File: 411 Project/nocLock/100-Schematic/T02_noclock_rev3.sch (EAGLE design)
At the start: 57 parts, among them J1 ICSP, J3 5BC-3-CA-F, J4 640455-2, J5 640455-2, J6 640455-2, J7 640455-2, J8 640455-2, Q1 DMN63D8LDW-7, Q3 DMG1012UW-7, U1 ATMEGA88A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

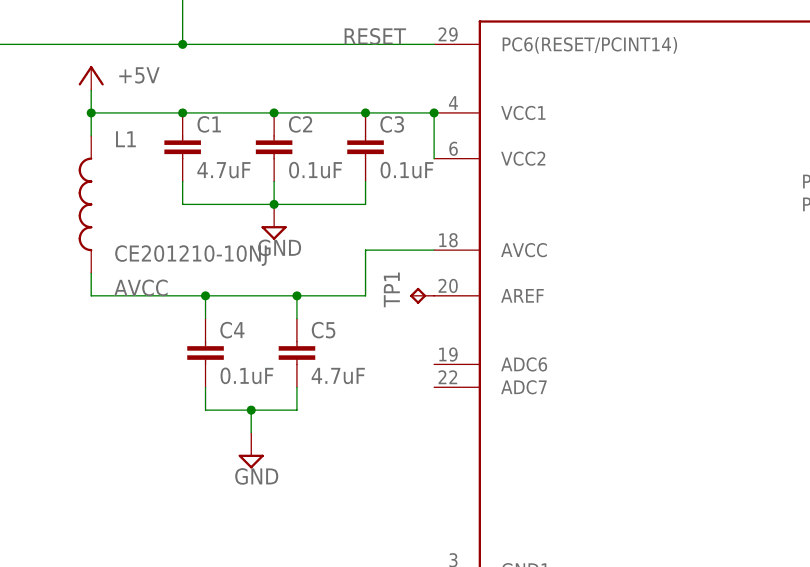
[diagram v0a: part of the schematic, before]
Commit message: Board revision
Fixed various issues with current layout, aded logo, and team name.
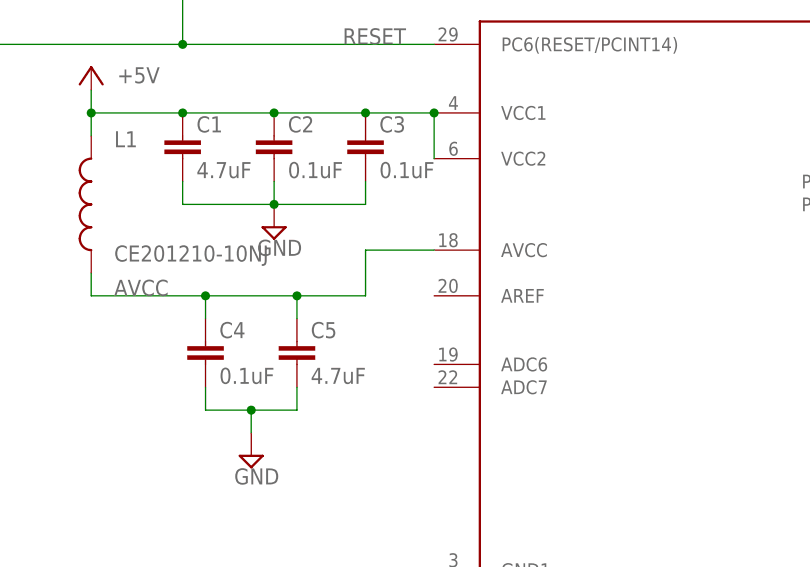
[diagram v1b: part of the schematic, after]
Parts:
- removed TP1: TPTP19R, testpad:TPTP19R
- U1: device nocLock_temp:ATMEGA88A -> T02_nocLock:ATMEGA88A; PARTNUM ATMEGA88A-AUR -> (none)
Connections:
- removed net N$13: TP1.TP, U1.AREF
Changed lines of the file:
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@@
 <parts>
 <part name="FRAME1" library="frames" deviceset="FRAME_B_L" device=""/>
-<part name="U1" library="nocLock_temp" deviceset="ATMEGA88A" device="">
-<attribute name="PARTNUM" value="ATMEGA88A-AUR "/>
-</part>
 <part name="P+2" library="supply1" deviceset="+5V" device=""/>
 <part name="C1" library="rcl" deviceset="C-EU" device="C0805" value="4.7uF">
@@
 <attribute name="PARTNUM" value="PMEG2005CT,215"/>
 </part>
-<part name="TP1" library="testpad" deviceset="TP" device="TP19R"/>
 <part name="SUPPLY18" library="supply2" deviceset="GND" device=""/>
 <part name="SUPPLY19" library="supply2" deviceset="GND" device=""/>
@@
 <part name="U$1" library="supply1" deviceset="+9V" device=""/>
 <part name="U$4" library="T02_nocLock" deviceset="+9V" device=""/>
+<part name="U1" library="T02_nocLock" deviceset="ATMEGA88A" device=""/>
 </parts>
 <sheets>
@@
 <instance part="FRAME1" gate="G$1" x="66.04" y="30.48"/>
 <instance part="FRAME1" gate="G$2" x="391.16" y="30.48"/>
-<instance part="U1" gate="G$1" x="266.7" y="180.34">
-<attribute name="PARTNUM" x="266.7" y="180.34" size="1.778" layer="96" display="off"/>
-</instance>
 <instance part="P+2" gate="1" x="193.04" y="208.28" smashed="yes">
 <attribute name="VALUE" x="200.66" y="208.28" size="1.778" layer="96" rot="R180"/>
@@
 <attribute name="PARTNUM" x="121.92" y="101.6" size="1.778" layer="96" display="off"/>
 </instance>
-<instance part="TP1" gate="G$1" x="228.6" y="182.88" rot="R90"/>
 <instance part="U2" gate="E" x="449.58" y="116.84"/>
 <instance part="U2" gate="F" x="449.58" y="88.9"/>
@@
 <instance part="U$1" gate="G$1" x="279.4" y="114.3"/>
 <instance part="U$4" gate="G$1" x="152.4" y="121.92"/>
+<instance part="U1" gate="G$1" x="266.7" y="180.34"/>
 </instances>
 <busses>
@@
 </segment>
 <segment>
-<pinref part="U1" gate="G$1" pin="GND1"/>
 <wire x1="231.14" y1="152.4" x2="228.6" y2="152.4" width="0.1524" layer="91"/>
 <wire x1="228.6" y1="152.4" x2="228.6" y2="149.86" width="0.1524" layer="91"/>
-<pinref part="U1" gate="G$1" pin="GND2"/>
 <wire x1="228.6" y1="149.86" x2="228.6" y2="147.32" width="0.1524" layer="91"/>
 <wire x1="228.6" y1="147.32" x2="228.6" y2="134.62" width="0.1524" layer="91"/>
 <wire x1="231.14" y1="149.86" x2="228.6" y2="149.86" width="0.1524" layer="91"/>
 <junction x="228.6" y="149.86"/>
-<pinref part="U1" gate="G$1" pin="GND3"/>
 <wire x1="228.6" y1="147.32" x2="231.14" y2="147.32" width="0.1524" layer="91"/>
 <junction x="228.6" y="147.32"/>
 <pinref part="SUPPLY14" gate="GND" pin="GND"/>
+<pinref part="U1" gate="G$1" pin="GND1"/>
+<pinref part="U1" gate="G$1" pin="GND2"/>
+<pinref part="U1" gate="G$1" pin="GND3"/>
 </segment>
 <segment>
@@
 <pinref part="P+2" gate="1" pin="+5V"/>
 <wire x1="193.04" y1="205.74" x2="193.04" y2="203.2" width="0.1524" layer="91"/>
-<pinref part="U1" gate="G$1" pin="VCC1"/>
 <wire x1="193.04" y1="203.2" x2="203.2" y2="203.2" width="0.1524" layer="91"/>
-<pinref part="U1" gate="G$1" pin="VCC2"/>
 <wire x1="203.2" y1="203.2" x2="213.36" y2="203.2" width="0.1524" layer="91"/>
 <wire x1="213.36" y1="203.2" x2="223.52" y2="203.2" width="0.1524" layer="91"/>
 <wire x1="223.52" y1="203.2" x2="231.14" y2="203.2" width="0.1524" layer="91"/>
 <wire x1="231.14" y1="198.12" x2="231.14" y2="203.2" width="0.1524" layer="91"/>
-<junction x="231.14" y="203.2"/>
 <pinref part="C1" gate="G$1" pin="1"/>
 <junction x="203.2" y="203.2"/>
@@
 <junction x="193.04" y="203.2"/>
 <pinref part="L1" gate="G$1" pin="2"/>
+<pinref part="U1" gate="G$1" pin="VCC1"/>
+<junction x="231.14" y="203.2"/>
+<pinref part="U1" gate="G$1" pin="VCC2"/>
 </segment>
 <segment>
@@
 <net name="AVCC" class="0">
 <segment>
-<pinref part="U1" gate="G$1" pin="AVCC"/>
 <wire x1="231.14" y1="187.96" x2="223.52" y2="187.96" width="0.1524" layer="91"/>
 <wire x1="193.04" y1="185.42" x2="193.04" y2="182.88" width="0.1524" layer="91"/>
@@
 <label x="195.58" y="182.88" size="1.778" layer="95"/>
 <pinref part="L1" gate="G$1" pin="1"/>
+<pinref part="U1" gate="G$1" pin="AVCC"/>
 </segment>
 </net>
@@
 <segment>
 <wire x1="180.34" y1="274.32" x2="180.34" y2="226.06" width="0.1524" layer="91"/>
-<pinref part="U1" gate="G$1" pin="PB0(PCINT0/CLKO/ICP1)"/>
 <pinref part="U2" gate="A" pin="O"/>
 <wire x1="180.34" y1="226.06" x2="307.34" y2="226.06" width="0.1524" layer="91"/>
@@
 <wire x1="307.34" y1="226.06" x2="307.34" y2="210.82" width="0.1524" layer="91"/>
 <wire x1="307.34" y1="210.82" x2="304.8" y2="210.82" width="0.1524" layer="91"/>
+<pinref part="U1" gate="G$1" pin="PB0(PCINT0/CLKO/ICP1)"/>
 </segment>
 </net>
@@
 <pinref part="R11" gate="G$1" pin="2"/>
 <label x="370.84" y="205.74" size="1.778" layer="95"/>
+<wire x1="304.8" y1="205.74" x2="396.24" y2="205.74" width="0.1524" layer="91"/>
 <pinref part="U1" gate="G$1" pin="PB2(PCINT2/SS/OC1B)"/>
-<wire x1="304.8" y1="205.74" x2="396.24" y2="205.74" width="0.1524" layer="91"/>
 </segment>
 </net>
@@
 <wire x1="231.14" y1="236.22" x2="231.14" y2="284.48" width="0.1524" layer="91"/>
 <wire x1="231.14" y1="284.48" x2="226.06" y2="284.48" width="0.1524" layer="91"/>
-<pinref part="U1" gate="G$1" pin="PB4(PCINT4/MISO)"/>
 <wire x1="304.8" y1="200.66" x2="325.12" y2="200.66" width="0.1524" layer="91"/>
 <wire x1="325.12" y1="200.66" x2="350.52" y2="200.66" width="0.1524" layer="91"/>
@@
 <wire x1="350.52" y1="200.66" x2="350.52" y2="99.06" width="0.1524" layer="91"/>
 <pinref part="J1" gate="G$1" pin="1"/>
+<pinref part="U1" gate="G$1" pin="PB4(PCINT4/MISO)"/>
 </segment>
 </net>
@@
 <net name="RESET" class="0">
 <segment>
-<pinref part="U1" gate="G$1" pin="PC6(RESET/PCINT14)"/>
 <wire x1="172.72" y1="210.82" x2="203.2" y2="210.82" width="0.1524" layer="91"/>
 <wire x1="203.2" y1="210.82" x2="231.14" y2="210.82" width="0.1524" layer="91"/>
@@
 <wire x1="172.72" y1="162.56" x2="162.56" y2="162.56" width="0.1524" layer="91"/>
 <pinref part="J1" gate="G$1" pin="5"/>
+<pinref part="U1" gate="G$1" pin="PC6(RESET/PCINT14)"/>
 </segment>
 </net>
 <net name="KNOCK_SENSE" class="0">
 <segment>
-<pinref part="U1" gate="G$1" pin="PC5(ADC5/SCL/PCINT13)"/>
 <wire x1="304.8" y1="172.72" x2="332.74" y2="172.72" width="0.1524" layer="91"/>
 <label x="307.34" y="172.72" size="1.778" layer="95"/>
@@
 <pinref part="J8" gate="G$1" pin="1"/>
 <wire x1="368.3" y1="279.4" x2="370.84" y2="279.4" width="0.1524" layer="91"/>
+<pinref part="U1" gate="G$1" pin="PC5(ADC5/SCL/PCINT13)"/>
 </segment>
 </net>
@@
 <net name="MOSI" class="0">
 <segment>
-<pinref part="U1" gate="G$1" pin="PB3(PCINT3/OC2A/MOSI)"/>
 <wire x1="304.8" y1="203.2" x2="320.04" y2="203.2" width="0.1524" layer="91"/>
 <wire x1="208.28" y1="231.14" x2="320.04" y2="231.14" width="0.1524" layer="91"/>
@@
 <wire x1="347.98" y1="134.62" x2="312.42" y2="134.62" width="0.1524" layer="91"/>
 <pinref part="J1" gate="G$1" pin="4"/>
+<pinref part="U1" gate="G$1" pin="PB3(PCINT3/OC2A/MOSI)"/>
 </segment>
 </net>
 <net name="SCK" class="0">
 <segment>
-<pinref part="U1" gate="G$1" pin="PB5(SCK/PCINT5)"/>
 <wire x1="304.8" y1="198.12" x2="322.58" y2="198.12" width="0.1524" layer="91"/>
 <wire x1="322.58" y1="198.12" x2="322.58" y2="233.68" width="0.1524" layer="91"/>
@@
 <wire x1="228.6" y1="279.4" x2="228.6" y2="233.68" width="0.1524" layer="91"/>
 <pinref part="J1" gate="G$1" pin="3"/>
+<pinref part="U1" gate="G$1" pin="PB5(SCK/PCINT5)"/>
 </segment>
 </net>
@@
 <segment>
 <wire x1="139.7" y1="215.9" x2="165.1" y2="215.9" width="0.1524" layer="91"/>
-<pinref part="U1" gate="G$1" pin="PB1(PCINT1/OC1A)"/>
 <wire x1="304.8" y1="208.28" x2="309.88" y2="208.28" width="0.1524" layer="91"/>
 <wire x1="309.88" y1="208.28" x2="309.88" y2="228.6" width="0.1524" layer="91"/>
@@
 <label x="259.08" y="228.6" size="1.778" layer="95"/>
 <pinref part="U2" gate="D" pin="O"/>
+<pinref part="U1" gate="G$1" pin="PB1(PCINT1/OC1A)"/>
 </segment>
 </net>
@@
 </segment>
 </net>
-<net name="N$13" class="0">
-<segment>
-<pinref part="U1" gate="G$1" pin="AREF"/>
-<pinref part="TP1" gate="G$1" pin="TP"/>
-</segment>
-</net>
